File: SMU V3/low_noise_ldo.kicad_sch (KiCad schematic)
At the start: 5 parts, among them U2 TPS7A2033PDBVR

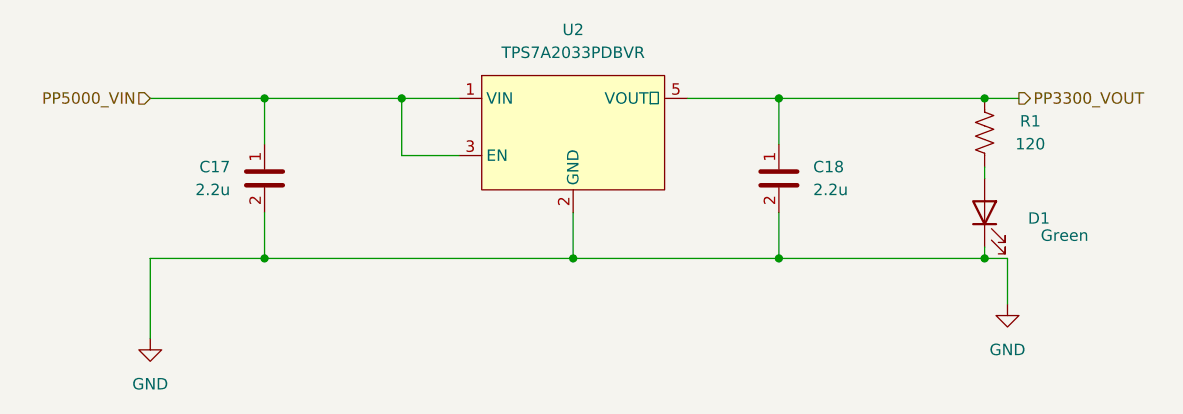
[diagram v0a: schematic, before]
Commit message: improved V3
added uart/spi test points and status leds
removed main 3v3 ldo
added silkscreen
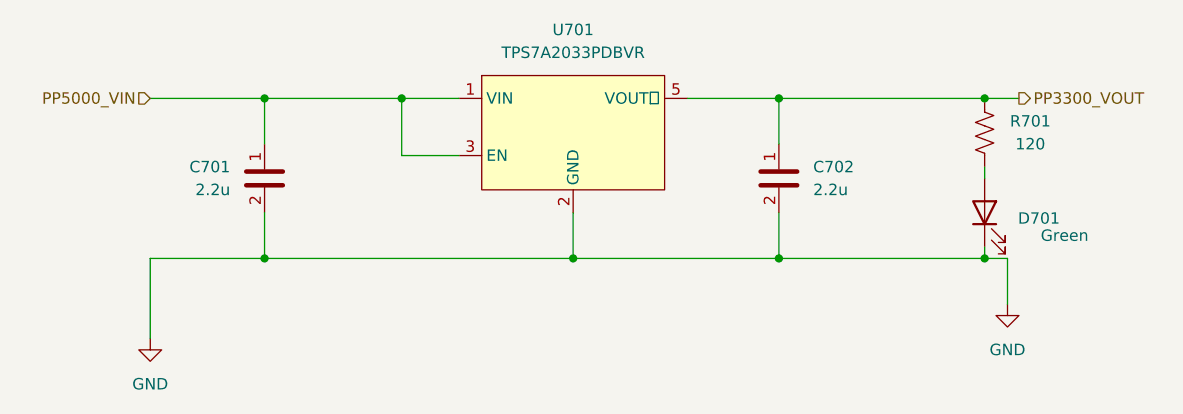
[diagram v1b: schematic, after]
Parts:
- renumbered C17 to C701, C18 to C702, D1 to D701, R1 to R701, U2 to U701
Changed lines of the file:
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@@
+	(wire
+		(pts
+			(xy 171.45 86.36) (xy 194.31 86.36)
+		)
+		(stroke
+			(width 0)
+			(type default)
+		)
+	)
 	(wire
 		(pts
@@
 		(pts
 			(xy 101.6 86.36) (xy 114.3 86.36)
-		)
-		(stroke
-			(width 0)
-			(type default)
-		)
-	)
-	(wire
-		(pts
-			(xy 171.45 86.36) (xy 194.31 86.36)
 		)
 		(stroke
@@
 		(dnp no)
 		(fields_autoplaced yes)
-		(property "Reference" "#PWR020"
+		(property "Reference" "#PWR0701"
 			(at 196.85 115.57 0)
 			(hide yes)
@@
 			(project "SMU V3"
 				(path "/1f58b889-96e6-4877-90a3-5a655db5910b/29d8e893-ab28-4f0b-b4ae-2fd3312ba121/39975dfb-3d32-4c42-b4f5-844dea62c3f9"
-					(reference "#PWR022")
+					(reference "#PWR0801")
 					(unit 1)
 				)
 				(path "/1f58b889-96e6-4877-90a3-5a655db5910b/29d8e893-ab28-4f0b-b4ae-2fd3312ba121/b244adf5-446c-45ea-af5d-14ac2e7aab9d"
-					(reference "#PWR020")
+					(reference "#PWR0701")
 					(unit 1)
 				)
 				(path "/1f58b889-96e6-4877-90a3-5a655db5910b/4cd2b3ee-b9d4-4006-b5a4-98c8a3d3240f/b3165549-ffd4-4aee-a330-81bb01c2c5f2"
-					(reference "#PWR024")
+					(reference "#PWR0901")
 					(unit 1)
 				)
@@
 		(in_pos_files yes)
 		(dnp no)
-		(property "Reference" "D1"
+		(property "Reference" "D701"
 			(at 200.3425 99.695 90)
 			(show_name no)
@@
 			(project "SMU V3"
 				(path "/1f58b889-96e6-4877-90a3-5a655db5910b/29d8e893-ab28-4f0b-b4ae-2fd3312ba121/39975dfb-3d32-4c42-b4f5-844dea62c3f9"
-					(reference "D2")
+					(reference "D801")
 					(unit 1)
 				)
 				(path "/1f58b889-96e6-4877-90a3-5a655db5910b/29d8e893-ab28-4f0b-b4ae-2fd3312ba121/b244adf5-446c-45ea-af5d-14ac2e7aab9d"
-					(reference "D1")
+					(reference "D701")
 					(unit 1)
 				)
 				(path "/1f58b889-96e6-4877-90a3-5a655db5910b/4cd2b3ee-b9d4-4006-b5a4-98c8a3d3240f/b3165549-ffd4-4aee-a330-81bb01c2c5f2"
-					(reference "D3")
+					(reference "D901")
 					(unit 1)
 				)
@@
 		(dnp no)
 		(fields_autoplaced yes)
-		(property "Reference" "C18"
+		(property "Reference" "C702"
 			(at 175.26 93.9799 0)
 			(show_name no)
@@
 			(project "SMU V3"
 				(path "/1f58b889-96e6-4877-90a3-5a655db5910b/29d8e893-ab28-4f0b-b4ae-2fd3312ba121/39975dfb-3d32-4c42-b4f5-844dea62c3f9"
-					(reference "C20")
+					(reference "C802")
 					(unit 1)
 				)
 				(path "/1f58b889-96e6-4877-90a3-5a655db5910b/29d8e893-ab28-4f0b-b4ae-2fd3312ba121/b244adf5-446c-45ea-af5d-14ac2e7aab9d"
-					(reference "C18")
+					(reference "C702")
 					(unit 1)
 				)
 				(path "/1f58b889-96e6-4877-90a3-5a655db5910b/4cd2b3ee-b9d4-4006-b5a4-98c8a3d3240f/b3165549-ffd4-4aee-a330-81bb01c2c5f2"
-					(reference "C22")
+					(reference "C902")
 					(unit 1)
 				)
@@
 		(in_pos_files yes)
 		(dnp no)
-		(property "Reference" "R1"
+		(property "Reference" "R701"
 			(at 199.39 88.9 90)
 			(show_name no)
@@
 			(project "SMU V3"
 				(path "/1f58b889-96e6-4877-90a3-5a655db5910b/29d8e893-ab28-4f0b-b4ae-2fd3312ba121/39975dfb-3d32-4c42-b4f5-844dea62c3f9"
-					(reference "R2")
+					(reference "R801")
 					(unit 1)
 				)
 				(path "/1f58b889-96e6-4877-90a3-5a655db5910b/29d8e893-ab28-4f0b-b4ae-2fd3312ba121/b244adf5-446c-45ea-af5d-14ac2e7aab9d"
-					(reference "R1")
+					(reference "R701")
 					(unit 1)
 				)
 				(path "/1f58b889-96e6-4877-90a3-5a655db5910b/4cd2b3ee-b9d4-4006-b5a4-98c8a3d3240f/b3165549-ffd4-4aee-a330-81bb01c2c5f2"
-					(reference "R3")
+					(reference "R901")
 					(unit 1)
 				)
@@
 		(dnp no)
 		(fields_autoplaced yes)
-		(property "Reference" "U2"
+		(property "Reference" "U701"
 			(at 148.59 78.74 0)
 			(show_name no)
@@
 			(project "SMU V3"
 				(path "/1f58b889-96e6-4877-90a3-5a655db5910b/29d8e893-ab28-4f0b-b4ae-2fd3312ba121/39975dfb-3d32-4c42-b4f5-844dea62c3f9"
-					(reference "U3")
+					(reference "U801")
 					(unit 1)
 				)
 				(path "/1f58b889-96e6-4877-90a3-5a655db5910b/29d8e893-ab28-4f0b-b4ae-2fd3312ba121/b244adf5-446c-45ea-af5d-14ac2e7aab9d"
-					(reference "U2")
+					(reference "U701")
 					(unit 1)
 				)
 				(path "/1f58b889-96e6-4877-90a3-5a655db5910b/4cd2b3ee-b9d4-4006-b5a4-98c8a3d3240f/b3165549-ffd4-4aee-a330-81bb01c2c5f2"
-					(reference "U4")
+					(reference "U901")
 					(unit 1)
 				)
@@
 		(in_pos_files yes)
 		(dnp no)
-		(property "Reference" "C17"
+		(property "Reference" "C701"
 			(at 110.49 93.9799 0)
 			(show_name no)
@@
 			(project "SMU V3"
 				(path "/1f58b889-96e6-4877-90a3-5a655db5910b/29d8e893-ab28-4f0b-b4ae-2fd3312ba121/39975dfb-3d32-4c42-b4f5-844dea62c3f9"
-					(reference "C19")
+					(reference "C801")
 					(unit 1)
 				)
 				(path "/1f58b889-96e6-4877-90a3-5a655db5910b/29d8e893-ab28-4f0b-b4ae-2fd3312ba121/b244adf5-446c-45ea-af5d-14ac2e7aab9d"
-					(reference "C17")
+					(reference "C701")
 					(unit 1)
 				)
 				(path "/1f58b889-96e6-4877-90a3-5a655db5910b/4cd2b3ee-b9d4-4006-b5a4-98c8a3d3240f/b3165549-ffd4-4aee-a330-81bb01c2c5f2"
-					(reference "C21")
+					(reference "C901")
 					(unit 1)
 				)
@@
 		(in_pos_files yes)
 		(dnp no)
-		(property "Reference" "#PWR019"
+		(property "Reference" "#PWR0702"
 			(at 101.6 119.38 0)
 			(hide yes)
@@
 			(project "SMU V3"
 				(path "/1f58b889-96e6-4877-90a3-5a655db5910b/29d8e893-ab28-4f0b-b4ae-2fd3312ba121/39975dfb-3d32-4c42-b4f5-844dea62c3f9"
-					(reference "#PWR021")
+					(reference "#PWR0802")
 					(unit 1)
 				)
 				(path "/1f58b889-96e6-4877-90a3-5a655db5910b/29d8e893-ab28-4f0b-b4ae-2fd3312ba121/b244adf5-446c-45ea-af5d-14ac2e7aab9d"
-					(reference "#PWR019")
+					(reference "#PWR0702")
 					(unit 1)
 				)
 				(path "/1f58b889-96e6-4877-90a3-5a655db5910b/4cd2b3ee-b9d4-4006-b5a4-98c8a3d3240f/b3165549-ffd4-4aee-a330-81bb01c2c5f2"
-					(reference "#PWR023")
-					(unit 1)
-				)
+					(reference "#PWR0902")
+					(unit 1)
+				)
